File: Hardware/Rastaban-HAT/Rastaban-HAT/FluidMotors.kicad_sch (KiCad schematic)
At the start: 10 parts, among them U3 TMC2208_Carrier, U4 TMC2208_Carrier

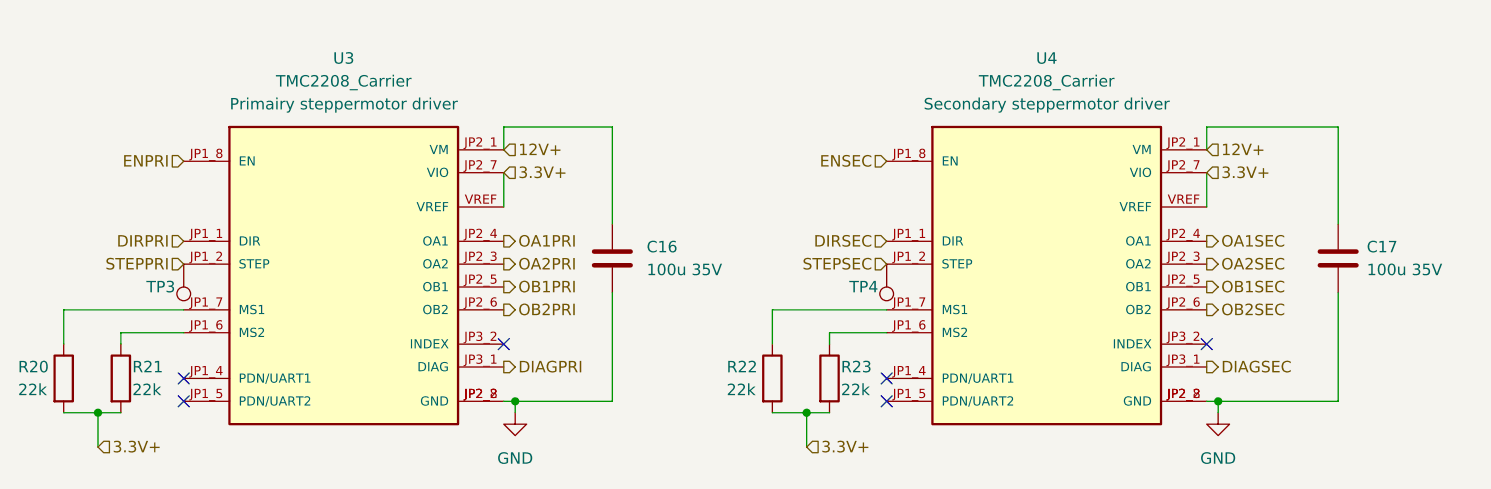
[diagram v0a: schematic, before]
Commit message: added 24V+ supply jumpers to prim and sec motors
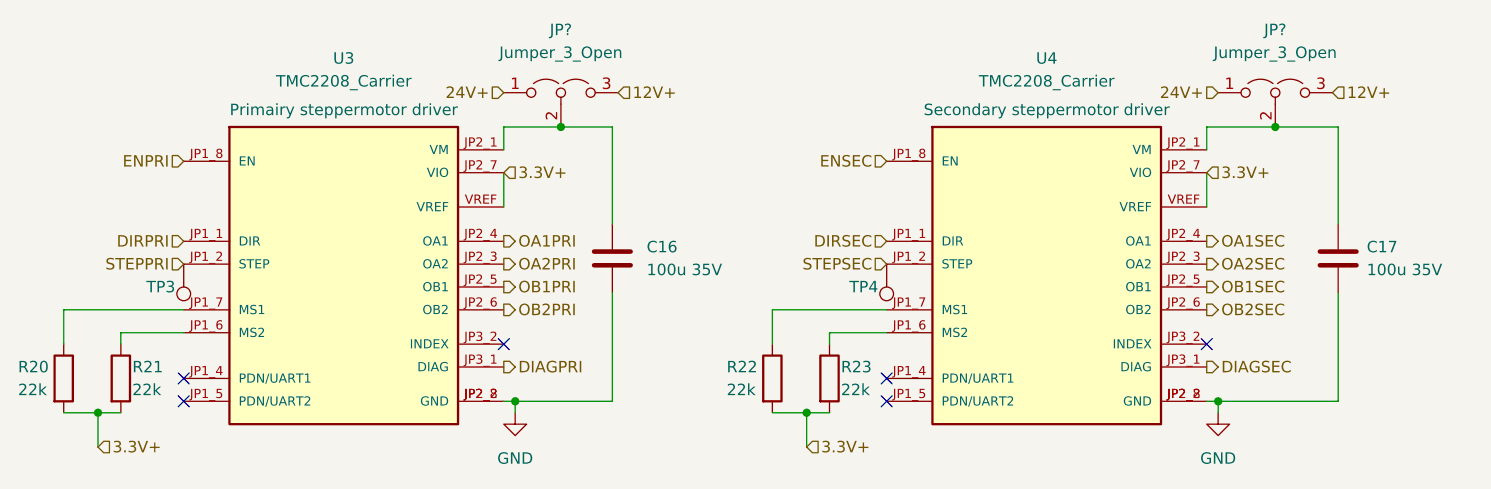
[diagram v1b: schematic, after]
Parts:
- added JP? (x2): Jumper_3_Open, symbol Jumper:Jumper_3_Open
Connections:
- net 12V+: now also JP?.3 (B), JP?.3 (B); no longer C16.1, C17.1, U3.JP2_1 (VM), U4.JP2_1 (VM)
- new net: C17.1, JP?.2 (C), U4.JP2_1 (VM)
- new net: C16.1, JP?.2 (C), U3.JP2_1 (VM)
- new net 24V+: JP?.1 (A), JP?.1 (A)
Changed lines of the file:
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@@
   (junction (at 157.48 118.11) (diameter 0) (color 0 0 0 0)
+  )
+  (junction (at 130.175 86.36) (diameter 0) (color 0 0 0 0)
+  )
+  (junction (at 209.55 86.36) (diameter 0) (color 0 0 0 0)
   )
   (junction (at 203.2 116.84) (diameter 0) (color 0 0 0 0)
@@
   (no_connect (at 88.265 116.84))
   (no_connect (at 166.37 116.84))
-  (wire (pts (xy 216.535 86.36) (xy 201.93 86.36))
+  (wire (pts (xy 216.535 86.36) (xy 209.55 86.36))
     (stroke (width 0) (type default) (color 0 0 0 0))
   )
@@
     (stroke (width 0) (type default) (color 0 0 0 0))
   )
+  (wire (pts (xy 130.175 86.36) (xy 123.825 86.36))
+    (stroke (width 0) (type default) (color 0 0 0 0))
+  )
   (wire (pts (xy 88.265 106.68) (xy 74.93 106.68))
     (stroke (width 0) (type default) (color 0 0 0 0))
@@
     (stroke (width 0) (type default) (color 0 0 0 0))
   )
-  (wire (pts (xy 135.89 86.36) (xy 123.825 86.36))
+  (wire (pts (xy 135.89 86.36) (xy 130.175 86.36))
     (stroke (width 0) (type default) (color 0 0 0 0))
   )
@@
     (stroke (width 0) (type default) (color 0 0 0 0))
   )
+  (wire (pts (xy 209.55 86.36) (xy 201.93 86.36))
+    (stroke (width 0) (type default) (color 0 0 0 0))
+  )
   (wire (pts (xy 135.89 86.36) (xy 135.89 97.155))
     (stroke (width 0) (type default) (color 0 0 0 0))
@@
     (effects (font (size 1.27 1.27)) (justify left))
   )
+  (hierarchical_label "24V+" (shape input) (at 123.825 82.55 180)
+    (effects (font (size 1.27 1.27)) (justify right))
+  )
   (hierarchical_label "DIAGPRI" (shape output) (at 123.825 113.03 0)
     (effects (font (size 1.27 1.27)) (justify left))
@@
     (effects (font (size 1.27 1.27)) (justify right))
   )
+  (hierarchical_label "24V+" (shape input) (at 203.2 82.55 180)
+    (effects (font (size 1.27 1.27)) (justify right))
+  )
   (hierarchical_label "OA2PRI" (shape output) (at 123.825 101.6 0)
     (effects (font (size 1.27 1.27)) (justify left))
   )
-  (hierarchical_label "12V+" (shape input) (at 123.825 88.9 0)
+  (hierarchical_label "12V+" (shape input) (at 136.525 82.55 0)
     (effects (font (size 1.27 1.27)) (justify left))
   )
@@
     (effects (font (size 1.27 1.27)) (justify left))
   )
-  (hierarchical_label "12V+" (shape input) (at 201.93 88.9 0)
+  (hierarchical_label "12V+" (shape input) (at 215.9 82.55 0)
     (effects (font (size 1.27 1.27)) (justify left))
   )
@@
       (effects (font (size 1.27 1.27)) (justify left bottom) hide)
     )
-    (property "Purpose" "Secondary steppermotor driver" (id 5) (at 184.15 83.82 0))
+    (property "Purpose" "Secondary steppermotor driver" (id 5) (at 184.15 84.455 0))
     (pin "JP1_1")
     (pin "JP1_2")
@@
     (pin "VREF")
   )
+  (symbol (lib_id "Jumper:Jumper_3_Open") (at 130.175 82.55 0) (unit 1)
+    (in_bom yes) (on_board yes) (fields_autoplaced)
+    (property "Reference" "JP?" (id 0) (at 130.175 75.565 0))
+    (property "Value" "Jumper_3_Open" (id 1) (at 130.175 78.105 0))
+    (property "Footprint" "" (id 2) (at 130.175 82.55 0)
+      (effects (font (size 1.27 1.27)) hide)
+    )
+    (property "Datasheet" "~" (id 3) (at 130.175 82.55 0)
+      (effects (font (size 1.27 1.27)) hide)
+    )
+    (pin "1")
+    (pin "2")
+    (pin "3")
+  )
   (symbol (lib_id "Device:R") (at 153.67 114.3 0) (unit 1)
     (in_bom yes) (on_board yes)
@@
     (pin "2")
   )
+  (symbol (lib_id "Jumper:Jumper_3_Open") (at 209.55 82.55 0) (unit 1)
+    (in_bom yes) (on_board yes) (fields_autoplaced)
+    (property "Reference" "JP?" (id 0) (at 209.55 75.565 0))
+    (property "Value" "Jumper_3_Open" (id 1) (at 209.55 78.105 0))
+    (property "Footprint" "" (id 2) (at 209.55 82.55 0)
+      (effects (font (size 1.27 1.27)) hide)
+    )
+    (property "Datasheet" "~" (id 3) (at 209.55 82.55 0)
+      (effects (font (size 1.27 1.27)) hide)
+    )
+    (pin "1")
+    (pin "2")
+    (pin "3")
+  )
   (symbol (lib_name "TMC2208_SILENTSTEPSTICK_1") (lib_id "TMC2208_SILENTSTEPSTICK:TMC2208_SILENTSTEPSTICK") (at 106.045 104.14 0) (unit 1)
-    (in_bom yes) (on_board yes) (fields_autoplaced)
+    (in_bom yes) (on_board yes)
     (property "Reference" "U3" (id 0) (at 106.045 78.74 0))
     (property "Value" "TMC2208_Carrier" (id 1) (at 106.045 81.28 0))
@@
       (effects (font (size 1.27 1.27)) (justify left bottom) hide)
     )
-    (property "Purpose" "Primairy steppermotor driver" (id 5) (at 106.045 83.82 0))
+    (property "Purpose" "Primairy steppermotor driver" (id 5) (at 106.045 84.455 0))
     (pin "JP1_1")
     (pin "JP1_2")

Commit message: enh layout
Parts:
- removed JP?: Jumper_3_Open, symbol Jumper:Jumper_3_Open
- added JP3: Jumper_3_Open, symbol Jumper:Jumper_3_Open
- JP2: renamed from JP?; Purpose (none) -> Choose between 12V/24V motor supply
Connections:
- net 12V+: now also JP3.3 (B)
- net 24V+: now also JP3.1 (A)
- net at C17.1, U4.JP2_1 (VM): now also JP3.2 (C)
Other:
- moved on the sheet: JP2
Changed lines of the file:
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@@
   (title_block
     (title "Rastaban-HAT")
+    (date "2022-09-27")
     (rev "1.1")
     (company "HAN")
@@
   (junction (at 157.48 118.11) (diameter 0) (color 0 0 0 0)
   )
-  (junction (at 130.175 86.36) (diameter 0) (color 0 0 0 0)
-  )
-  (junction (at 209.55 86.36) (diameter 0) (color 0 0 0 0)
+  (junction (at 211.455 86.36) (diameter 0) (color 0 0 0 0)
   )
   (junction (at 203.2 116.84) (diameter 0) (color 0 0 0 0)
   )
   (junction (at 125.095 116.84) (diameter 0) (color 0 0 0 0)
+  )
+  (junction (at 132.715 86.36) (diameter 0) (color 0 0 0 0)
   )
   (junction (at 78.74 118.11) (diameter 0) (color 0 0 0 0)
@@
   (no_connect (at 88.265 116.84))
   (no_connect (at 166.37 116.84))
-  (wire (pts (xy 216.535 86.36) (xy 209.55 86.36))
+  (wire (pts (xy 201.93 86.36) (xy 211.455 86.36))
     (stroke (width 0) (type default) (color 0 0 0 0))
   )
@@
     (stroke (width 0) (type default) (color 0 0 0 0))
   )
-  (wire (pts (xy 130.175 86.36) (xy 123.825 86.36))
+  (wire (pts (xy 123.825 86.36) (xy 132.715 86.36))
     (stroke (width 0) (type default) (color 0 0 0 0))
   )
@@
     (stroke (width 0) (type default) (color 0 0 0 0))
   )
+  (wire (pts (xy 211.455 86.36) (xy 216.535 86.36))
+    (stroke (width 0) (type default) (color 0 0 0 0))
+  )
   (wire (pts (xy 78.74 118.11) (xy 78.74 121.92))
     (stroke (width 0) (type default) (color 0 0 0 0))
@@
     (stroke (width 0) (type default) (color 0 0 0 0))
   )
-  (wire (pts (xy 135.89 86.36) (xy 130.175 86.36))
+  (wire (pts (xy 135.89 86.36) (xy 132.715 86.36))
     (stroke (width 0) (type default) (color 0 0 0 0))
   )
@@
     (stroke (width 0) (type default) (color 0 0 0 0))
   )
-  (wire (pts (xy 209.55 86.36) (xy 201.93 86.36))
-    (stroke (width 0) (type default) (color 0 0 0 0))
-  )
   (wire (pts (xy 135.89 86.36) (xy 135.89 97.155))
     (stroke (width 0) (type default) (color 0 0 0 0))
@@
     (effects (font (size 1.27 1.27)) (justify left))
   )
-  (hierarchical_label "24V+" (shape input) (at 123.825 82.55 180)
+  (hierarchical_label "24V+" (shape input) (at 126.365 82.55 180)
     (effects (font (size 1.27 1.27)) (justify right))
   )
@@
     (effects (font (size 1.27 1.27)) (justify right))
   )
+  (hierarchical_label "12V+" (shape input) (at 217.805 82.55 0)
+    (effects (font (size 1.27 1.27)) (justify left))
+  )
   (hierarchical_label "OA1SEC" (shape output) (at 201.93 99.06 0)
     (effects (font (size 1.27 1.27)) (justify left))
@@
     (effects (font (size 1.27 1.27)) (justify right))
   )
-  (hierarchical_label "24V+" (shape input) (at 203.2 82.55 180)
+  (hierarchical_label "24V+" (shape input) (at 205.105 82.55 180)
     (effects (font (size 1.27 1.27)) (justify right))
   )
@@
     (effects (font (size 1.27 1.27)) (justify left))
   )
-  (hierarchical_label "12V+" (shape input) (at 136.525 82.55 0)
+  (hierarchical_label "12V+" (shape input) (at 139.065 82.55 0)
     (effects (font (size 1.27 1.27)) (justify left))
   )
@@
   )
   (hierarchical_label "3.3V+" (shape input) (at 201.93 91.44 0)
-    (effects (font (size 1.27 1.27)) (justify left))
-  )
-  (hierarchical_label "12V+" (shape input) (at 215.9 82.55 0)
     (effects (font (size 1.27 1.27)) (justify left))
   )
@@
     (pin "VREF")
   )
-  (symbol (lib_id "Jumper:Jumper_3_Open") (at 130.175 82.55 0) (unit 1)
-    (in_bom yes) (on_board yes) (fields_autoplaced)
-    (property "Reference" "JP?" (id 0) (at 130.175 75.565 0))
-    (property "Value" "Jumper_3_Open" (id 1) (at 130.175 78.105 0))
-    (property "Footprint" "" (id 2) (at 130.175 82.55 0)
-      (effects (font (size 1.27 1.27)) hide)
-    )
-    (property "Datasheet" "~" (id 3) (at 130.175 82.55 0)
-      (effects (font (size 1.27 1.27)) hide)
+  (symbol (lib_id "Jumper:Jumper_3_Open") (at 132.715 82.55 0) (unit 1)
+    (in_bom yes) (on_board yes)
+    (property "Reference" "JP2" (id 0) (at 132.715 75.565 0))
+    (property "Value" "Jumper_3_Open" (id 1) (at 132.715 78.105 0))
+    (property "Footprint" "" (id 2) (at 132.715 82.55 0)
+      (effects (font (size 1.27 1.27)) hide)
+    )
+    (property "Datasheet" "~" (id 3) (at 132.715 82.55 0)
+      (effects (font (size 1.27 1.27)) hide)
+    )
+    (property "Purpose" "Choose between 12V/24V motor supply" (id 4) (at 132.715 80.01 0)
+      (effects (font (size 0.8 0.8)))
     )
     (pin "1")
@@
     (pin "1")
     (pin "2")
+  )
+  (symbol (lib_id "Jumper:Jumper_3_Open") (at 211.455 82.55 0) (unit 1)
+    (in_bom yes) (on_board yes)
+    (property "Reference" "JP3" (id 0) (at 211.455 75.565 0))
+    (property "Value" "Jumper_3_Open" (id 1) (at 211.455 78.105 0))
+    (property "Footprint" "" (id 2) (at 211.455 82.55 0)
+      (effects (font (size 1.27 1.27)) hide)
+    )
+    (property "Datasheet" "~" (id 3) (at 211.455 82.55 0)
+      (effects (font (size 1.27 1.27)) hide)
+    )
+    (property "Purpose" "Choose between 12V/24V motor supply" (id 4) (at 211.455 80.01 0)
+      (effects (font (size 0.8 0.8)))
+    )
+    (pin "1")
+    (pin "2")
+    (pin "3")
   )
   (symbol (lib_id "Device:R") (at 81.28 114.3 0) (unit 1)
@@
     (pin "2")
   )
-  (symbol (lib_id "Jumper:Jumper_3_Open") (at 209.55 82.55 0) (unit 1)
-    (in_bom yes) (on_board yes) (fields_autoplaced)
-    (property "Reference" "JP?" (id 0) (at 209.55 75.565 0))
-    (property "Value" "Jumper_3_Open" (id 1) (at 209.55 78.105 0))
-    (property "Footprint" "" (id 2) (at 209.55 82.55 0)
-      (effects (font (size 1.27 1.27)) hide)
-    )
-    (property "Datasheet" "~" (id 3) (at 209.55 82.55 0)
-      (effects (font (size 1.27 1.27)) hide)
-    )
-    (pin "1")
-    (pin "2")
-    (pin "3")
-  )
   (symbol (lib_name "TMC2208_SILENTSTEPSTICK_1") (lib_id "TMC2208_SILENTSTEPSTICK:TMC2208_SILENTSTEPSTICK") (at 106.045 104.14 0) (unit 1)

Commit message: Schematic v1.2
added johan brussen's advice
written software for stepper motor drivers
test report written.
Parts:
- added C22, C23: 100nF, symbol Device:C
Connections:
- net 3.3V+: now also C22.1, C22.2, C23.1, C23.2
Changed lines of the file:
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@@
     (title "Rastaban-HAT")
     (date "2022-09-27")
-    (rev "1.1")
+    (rev "1.2")
     (company "HAN")
     (comment 1 "Casper R. Tak")
   )
+  (junction (at 201.93 95.25) (diameter 0) (color 0 0 0 0)
+  )
+  (junction (at 201.93 91.44) (diameter 0) (color 0 0 0 0)
+  )
   (junction (at 157.48 118.11) (diameter 0) (color 0 0 0 0)
   )
   (junction (at 211.455 86.36) (diameter 0) (color 0 0 0 0)
   )
+  (junction (at 123.825 91.44) (diameter 0) (color 0 0 0 0)
+  )
   (junction (at 203.2 116.84) (diameter 0) (color 0 0 0 0)
+  )
+  (junction (at 123.825 95.25) (diameter 0) (color 0 0 0 0)
   )
   (junction (at 125.095 116.84) (diameter 0) (color 0 0 0 0)
@@
     (stroke (width 0) (type default) (color 0 0 0 0))
   )
+  (wire (pts (xy 123.825 95.25) (xy 123.825 97.155))
+    (stroke (width 0) (type default) (color 0 0 0 0))
+  )
   (wire (pts (xy 216.535 116.84) (xy 216.535 104.775))
     (stroke (width 0) (type default) (color 0 0 0 0))
@@
     (stroke (width 0) (type default) (color 0 0 0 0))
   )
+  (wire (pts (xy 201.93 95.25) (xy 201.93 97.155))
+    (stroke (width 0) (type default) (color 0 0 0 0))
+  )
+  (wire (pts (xy 201.93 89.535) (xy 210.185 89.535))
+    (stroke (width 0) (type default) (color 0 0 0 0))
+  )
   (wire (pts (xy 201.93 86.36) (xy 201.93 88.9))
     (stroke (width 0) (type default) (color 0 0 0 0))
@@
     (stroke (width 0) (type default) (color 0 0 0 0))
   )
+  (wire (pts (xy 201.93 91.44) (xy 201.93 89.535))
+    (stroke (width 0) (type default) (color 0 0 0 0))
+  )
+  (wire (pts (xy 123.825 89.535) (xy 132.08 89.535))
+    (stroke (width 0) (type default) (color 0 0 0 0))
+  )
+  (wire (pts (xy 123.825 91.44) (xy 123.825 89.535))
+    (stroke (width 0) (type default) (color 0 0 0 0))
+  )
   (wire (pts (xy 153.67 106.68) (xy 166.37 106.68))
     (stroke (width 0) (type default) (color 0 0 0 0))
@@
     (stroke (width 0) (type default) (color 0 0 0 0))
   )
+  (wire (pts (xy 123.825 97.155) (xy 132.08 97.155))
+    (stroke (width 0) (type default) (color 0 0 0 0))
+  )
   (wire (pts (xy 203.2 118.11) (xy 203.2 116.84))
     (stroke (width 0) (type default) (color 0 0 0 0))
@@
   )
   (wire (pts (xy 125.095 116.84) (xy 123.825 116.84))
+    (stroke (width 0) (type default) (color 0 0 0 0))
+  )
+  (wire (pts (xy 201.93 97.155) (xy 210.185 97.155))
     (stroke (width 0) (type default) (color 0 0 0 0))
   )
@@
     (pin "3")
   )
+  (symbol (lib_id "Device:C") (at 210.185 93.345 0) (unit 1)
+    (in_bom yes) (on_board yes) (fields_autoplaced)
+    (property "Reference" "C23" (id 0) (at 213.36 92.0749 0)
+      (effects (font (size 1.27 1.27)) (justify left))
+    )
+    (property "Value" "100nF" (id 1) (at 213.36 94.6149 0)
+      (effects (font (size 1.27 1.27)) (justify left))
+    )
+    (property "Footprint" "" (id 2) (at 211.1502 97.155 0)
+      (effects (font (size 1.27 1.27)) hide)
+    )
+    (property "Datasheet" "~" (id 3) (at 210.185 93.345 0)
+      (effects (font (size 1.27 1.27)) hide)
+    )
+    (pin "1")
+    (pin "2")
+  )
   (symbol (lib_id "Device:R") (at 81.28 114.3 0) (unit 1)
     (in_bom yes) (on_board yes)
@@
     (pin "1")
   )
+  (symbol (lib_id "Device:C") (at 132.08 93.345 0) (unit 1)
+    (in_bom yes) (on_board yes) (fields_autoplaced)
+    (property "Reference" "C22" (id 0) (at 135.89 92.0749 0)
+      (effects (font (size 1.27 1.27)) (justify left))
+    )
+    (property "Value" "100nF" (id 1) (at 135.89 94.6149 0)
+      (effects (font (size 1.27 1.27)) (justify left))
+    )
+    (property "Footprint" "" (id 2) (at 133.0452 97.155 0)
+      (effects (font (size 1.27 1.27)) hide)
+    )
+    (property "Datasheet" "~" (id 3) (at 132.08 93.345 0)
+      (effects (font (size 1.27 1.27)) hide)
+    )
+    (pin "1")
+    (pin "2")
+  )
 )
